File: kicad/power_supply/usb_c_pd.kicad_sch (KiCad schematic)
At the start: 39 parts, among them J201 Conn_01x04_Socket, J202 12401826E412A, J203 Conn_01x03_Socket, SW201 SW_SPST, U201 USBLC6-2SC6, U202 STUSB4500QTR

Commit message: psu buck-boost schematic capture
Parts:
- removed J203: Conn_01x03_Socket, symbol Connector:Conn_01x03_Socket
- added J203: USB IDC, symbol Connector:Conn_01x05_Pin
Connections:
- net D_N: now also J203.2 (Pin_2)
- net D_P: now also J203.3 (Pin_3)
- net GND: now also J203.4 (Pin_4), J203.5 (Pin_5)
- no-connect marks 12 -> 13
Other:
- note added: "Black"
- note added: "Green"
- note added: "Red"
- note added: "White"
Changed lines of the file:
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@@
 	)
 	(junction
+		(at 140.97 184.15)
+		(diameter 0)
+		(color 0 0 0 0)
+	)
+	(junction
 		(at 227.33 43.18)
 		(diameter 0)
@@
 	)
 	(no_connect
+		(at 139.7 173.99)
+	)
+	(no_connect
 		(at 137.16 130.81)
 	)
@@
 	(wire
 		(pts
-			(xy 142.24 179.07) (xy 135.89 179.07)
+			(xy 146.05 179.07) (xy 139.7 179.07)
 		)
 		(stroke
@@
 	(wire
 		(pts
+			(xy 140.97 181.61) (xy 140.97 184.15)
+		)
+		(stroke
+			(width 0)
+			(type default)
+		)
+	)
+	(wire
+		(pts
 			(xy 90.17 35.56) (xy 85.09 35.56)
 		)
@@
 	(wire
 		(pts
-			(xy 142.24 176.53) (xy 135.89 176.53)
+			(xy 146.05 176.53) (xy 139.7 176.53)
 		)
 		(stroke
@@
 	(wire
 		(pts
+			(xy 139.7 181.61) (xy 140.97 181.61)
+		)
+		(stroke
+			(width 0)
+			(type default)
+		)
+	)
+	(wire
+		(pts
 			(xy 22.86 39.37) (xy 22.86 40.64)
 		)
@@
 	(wire
 		(pts
-			(xy 135.89 181.61) (xy 137.16 181.61)
+			(xy 139.7 184.15) (xy 140.97 184.15)
 		)
 		(stroke
@@
 	(wire
 		(pts
-			(xy 137.16 181.61) (xy 137.16 182.88)
+			(xy 140.97 184.15) (xy 140.97 185.42)
 		)
 		(stroke
@@
 		)
 	)
+	(text "Black"
+		(exclude_from_sim no)
+		(at 131.318 184.404 0)
+		(effects
+			(font
+				(size 1.27 1.27)
+			)
+		)
+	)
+	(text "Green"
+		(exclude_from_sim no)
+		(at 131.318 179.324 0)
+		(effects
+			(font
+				(size 1.27 1.27)
+			)
+		)
+	)
 	(text "Reset Switch"
 		(exclude_from_sim no)
@@
 		)
 	)
+	(text "Red"
+		(exclude_from_sim no)
+		(at 130.556 174.244 0)
+		(effects
+			(font
+				(size 1.27 1.27)
+			)
+		)
+	)
 	(text "USB Header"
 		(exclude_from_sim no)
@@
 		)
 	)
+	(text "Black"
+		(exclude_from_sim no)
+		(at 131.318 181.864 0)
+		(effects
+			(font
+				(size 1.27 1.27)
+			)
+		)
+	)
+	(text "White"
+		(exclude_from_sim no)
+		(at 131.318 176.784 0)
+		(effects
+			(font
+				(size 1.27 1.27)
+			)
+		)
+	)
 	(text "ADDR0 | ADDR1 | Address\n  0    |   0    | 0x28*\n  0    |   1    | 0x29\n  1    |   0    | 0x2A\n  1    |   1    | 0x2B\n\n*: Default\n0: Jumper closed\n1: Jumper open"
 		(exclude_from_sim no)
@@
 	)
 	(label "D_P"
-		(at 142.24 179.07 180)
+		(at 146.05 179.07 180)
 		(fields_autoplaced yes)
 		(effects
@@
 	)
 	(label "D_N"
-		(at 142.24 176.53 180)
+		(at 146.05 176.53 180)
 		(fields_autoplaced yes)
 		(effects
@@
 	)
 	(symbol
+		(lib_id "Connector:Conn_01x05_Pin")
+		(at 134.62 179.07 0)
+		(unit 1)
+		(exclude_from_sim no)
+		(in_bom yes)
+		(on_board yes)
+		(dnp no)
+		(property "Reference" "J203"
+			(at 135.382 168.148 0)
+			(effects
+				(font
+					(size 1.27 1.27)
+				)
+			)
+		)
+		(property "Value" "USB IDC"
+			(at 135.382 170.688 0)
+			(effects
+				(font
+					(size 1.27 1.27)
+				)
+			)
+		)
+		(property "Footprint" ""
+			(at 134.62 179.07 0)
+			(effects
+				(font
+					(size 1.27 1.27)
+				)
+				(hide yes)
+			)
+		)
+		(property "Datasheet" "~"
+			(at 134.62 179.07 0)
+			(effects
+				(font
+					(size 1.27 1.27)
+				)
+				(hide yes)
+			)
+		)
+		(property "Description" "Generic connector, single row, 01x05, script generated"
+			(at 134.62 179.07 0)
+			(effects
+				(font
+					(size 1.27 1.27)
+				)
+				(hide yes)
+			)
+		)
+		(pin "3"
+		)
+		(pin "1"
+		)
+		(pin "4"
+		)
+		(pin "2"
+		)
+		(pin "5"
+		)
+		(instances
+			(project ""
+				(path "/6a7d9dc9-f78f-470f-911b-b95256023173/4a384965-6a35-4bf6-849e-cb865e62d5b4"
+					(reference "J203")
+					(unit 1)
+				)
+			)
+		)
+	)
+	(symbol
 		(lib_id "Device:R_Small_US")
 		(at 260.35 57.15 0)
@@
 	(symbol
 		(lib_id "power:GND")
-		(at 137.16 182.88 0)
+		(at 140.97 185.42 0)
 		(unit 1)
 		(exclude_from_sim no)
@@
 		(fields_autoplaced yes)
 		(property "Reference" "#PWR0206"
-			(at 137.16 189.23 0)
+			(at 140.97 191.77 0)
 			(effects
 				(font
@@
 		)
 		(property "Value" "GND"
-			(at 137.16 187.96 0)
+			(at 140.97 190.5 0)
 			(effects
 				(font
@@
 		)
 		(property "Footprint" ""
-			(at 137.16 182.88 0)
+			(at 140.97 185.42 0)
 			(effects
 				(font
@@
 		)
 		(property "Datasheet" ""
-			(at 137.16 182.88 0)
+			(at 140.97 185.42 0)
 			(effects
 				(font
@@
 		)
 		(property "Description" "Power symbol creates a global label with name \"GND\" , ground"
-			(at 137.16 182.88 0)
+			(at 140.97 185.42 0)
 			(effects
 				(font
@@
 					(unit 1)
 				)
-			)
-		)
-	)
-	(symbol
-		(lib_id "Connector:Conn_01x03_Socket")
-		(at 130.81 179.07 180)
-		(unit 1)
-		(exclude_from_sim no)
-		(in_bom yes)
-		(on_board yes)
-		(dnp no)
-		(property "Reference" "J203"
-			(at 133.35 172.466 0)
-			(effects
-				(font
-					(size 1.27 1.27)
-				)
-			)
-		)
-		(property "Value" "Conn_01x03_Socket"
-			(at 131.445 173.99 0)
-			(effects
-				(font
-					(size 1.27 1.27)
-				)
-				(hide yes)
-			)
-		)
-		(property "Footprint" ""
-			(at 130.81 179.07 0)
-			(effects
-				(font
-					(size 1.27 1.27)
-				)
-				(hide yes)
-			)
-		)
-		(property "Datasheet" "~"
-			(at 130.81 179.07 0)
-			(effects
-				(font
-					(size 1.27 1.27)
-				)
-				(hide yes)
-			)
-		)
-		(property "Description" "Generic connector, single row, 01x03, script generated"
-			(at 130.81 179.07 0)
-			(effects
-				(font
-					(size 1.27 1.27)
-				)
-				(hide yes)
-			)
-		)
-		(pin "3"
-		)
-		(pin "1"
-		)
-		(pin "2"
-		)
-		(instances
-			(project ""
-				(path "/6a7d9dc9-f78f-470f-911b-b95256023173/4a384965-6a35-4bf6-849e-cb865e62d5b4"
-					(reference "J203")
-					(unit 1)
-				)

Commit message: schematic capture
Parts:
- J202: MPN (none) -> 12401826E412A
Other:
- moved on the sheet: TP201
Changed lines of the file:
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@@
 	(wire
 		(pts
-			(xy 161.29 101.6) (xy 171.45 101.6)
+			(xy 163.83 101.6) (xy 171.45 101.6)
 		)
 		(stroke
@@
 	)
 	(symbol
-		(lib_name "SISA35DN-T1-GE3_1")
 		(lib_id "SISA35DN-T1-GE3:SISA35DN-T1-GE3")
 		(at 220.98 45.72 270)
@@
 		(on_board yes)
 		(dnp no)
-		(fields_autoplaced yes)
 		(property "Reference" "J202"
 			(at 121.92 67.31 0)
@@
 					(size 1.27 1.27)
 				)
+				(hide yes)
 			)
 		)
@@
 			)
 		)
-		(property "Datasheet" "https://www.usb.org/sites/default/files/documents/usb_type-c.zip"
+		(property "Datasheet" "https://cdn.amphenol-cs.com/media/wysiwyg/files/documentation/datasheet/inputoutput/io_usb_type_c.pdf"
 			(at 125.73 100.33 0)
 			(effects
@@
 			)
 		)
-		(property "Description" "USB Full-Featured Type-C Receptacle connector"
+		(property "Description" "CONN RCP USB3.1 TYPEC 24P SMD RA"
 			(at 121.92 100.33 0)
 			(effects
@@
 			)
 		)
+		(property "MPN" "12401826E412A"
+			(at 121.92 70.358 0)
+			(effects
+				(font
+					(size 1.27 1.27)
+				)
+			)
+		)
 		(pin "A2"
 		)
@@
 	(symbol
 		(lib_id "Connector:TestPoint")
-		(at 161.29 101.6 90)
+		(at 163.83 101.6 90)
 		(unit 1)
 		(exclude_from_sim no)
@@
 		(dnp no)
 		(property "Reference" "TP201"
-			(at 156.464 101.6 90)
+			(at 159.004 101.6 90)
 			(effects
 				(font
@@
 		)
 		(property "Value" "TestPoint"
-			(at 156.21 100.3301 90)
+			(at 158.75 100.3301 90)
 			(effects
 				(font
@@
 		)
 		(property "Footprint" ""
-			(at 161.29 96.52 0)
+			(at 163.83 96.52 0)
 			(effects
 				(font
@@
 		)
 		(property "Datasheet" "~"
-			(at 161.29 96.52 0)
+			(at 163.83 96.52 0)
 			(effects
 				(font
@@
 		)
 		(property "Description" "test point"
-			(at 161.29 101.6 0)
+			(at 163.83 101.6 0)
 			(effects
 				(font

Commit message: schematic capture
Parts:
- removed TP202, TP203: TestPoint, symbol Connector:TestPoint
- renumbered TP204 to TP202, TP205 to TP203, TP206 to TP204
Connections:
- net POWER_OK3_OD: now reaches U202.14 (POWER_OK3)
- net POWER_OK2_OD: now reaches U202.20 (POWER_OK2)
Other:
- note added: "Required PDO configuration: PDO1 = Doesn't matter, the minimum VIN for the MP2759 is 6.6V to charge a 1-cell battery PDO2 = 9V, 2A (18W, 1-cell max.) PDO3 = 15V, 2A (30W, 3-cell max.) **Make sure to set the charger ILIM to the lowest current of PDO2 and PDO3**"
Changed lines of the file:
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@@
 		)
 	)
+	(text "Required PDO configuration:\n\nPDO1 = Doesn't matter, the minimum \n		VIN for the MP2759 is 6.6V \n		to charge a 1-cell battery\nPDO2 = 9V, 2A (18W, 1-cell max.)\nPDO3 = 15V, 2A (30W, 3-cell max.)\n\n\n**Make sure to set the charger ILIM\nto the lowest current of PDO2 and PDO3**"
+		(exclude_from_sim no)
+		(at 214.63 125.73 0)
+		(effects
+			(font
+				(size 1.905 1.905)
+			)
+			(justify left top)
+		)
+	)
 	(text "White"
 		(exclude_from_sim no)
@@
 		)
 	)
-	(hierarchical_label "VSNK"
+	(hierarchical_label "POWER_OK3_OD"
 		(shape input)
+		(at 204.47 88.9 0)
+		(fields_autoplaced yes)
+		(effects
+			(font
+				(size 1.27 1.27)
+			)
+			(justify left)
+		)
+	)
+	(hierarchical_label "POWER_OK2_OD"
+		(shape input)
+		(at 204.47 86.36 0)
+		(fields_autoplaced yes)
+		(effects
+			(font
+				(size 1.27 1.27)
+			)
+			(justify left)
+		)
+	)
+	(hierarchical_label "VSNK"
+		(shape output)
 		(at 267.97 43.18 0)
 		(fields_autoplaced yes)
@@
 		(on_board yes)
 		(dnp no)
-		(property "Reference" "TP206"
+		(property "Reference" "TP204"
 			(at 209.296 104.14 90)
 			(effects
@@
 			(project "power_supply"
 				(path "/6a7d9dc9-f78f-470f-911b-b95256023173/4a384965-6a35-4bf6-849e-cb865e62d5b4"
-					(reference "TP206")
+					(reference "TP204")
 					(unit 1)
 				)
@@
 		(on_board yes)
 		(dnp no)
-		(property "Reference" "TP205"
+		(property "Reference" "TP203"
 			(at 209.296 101.6 90)
 			(effects
@@
 			(project "power_supply"
 				(path "/6a7d9dc9-f78f-470f-911b-b95256023173/4a384965-6a35-4bf6-849e-cb865e62d5b4"
-					(reference "TP205")
+					(reference "TP203")
 					(unit 1)
 				)
@@
 	)
 	(symbol
-		(lib_id "Connector:TestPoint")
-		(at 204.47 88.9 270)
-		(unit 1)
-		(exclude_from_sim no)
-		(in_bom yes)
-		(on_board yes)
-		(dnp no)
-		(property "Reference" "TP203"
-			(at 209.296 88.9 90)
-			(effects
-				(font
-					(size 1.27 1.27)
-				)
-				(justify left)
-			)
-		)
-		(property "Value" "TestPoint"
-			(at 209.55 90.1699 90)
-			(effects
-				(font
-					(size 1.27 1.27)
-				)
-				(justify left)
-				(hide yes)
-			)
-		)
-		(property "Footprint" ""
-			(at 204.47 93.98 0)
-			(effects
-				(font
-					(size 1.27 1.27)
-				)
-				(hide yes)
-			)
-		)
-		(property "Datasheet" "~"
-			(at 204.47 93.98 0)
-			(effects
-				(font
-					(size 1.27 1.27)
-				)
-				(hide yes)
-			)
-		)
-		(property "Description" "test point"
-			(at 204.47 88.9 0)
-			(effects
-				(font
-					(size 1.27 1.27)
-				)
-				(hide yes)
-			)
-		)
-		(pin "1"
-		)
-		(instances
-			(project "power_supply"
-				(path "/6a7d9dc9-f78f-470f-911b-b95256023173/4a384965-6a35-4bf6-849e-cb865e62d5b4"
-					(reference "TP203")
-					(unit 1)
-				)
-			)
-		)
-	)
-	(symbol
 		(lib_id "power:GND")
 		(at 209.55 66.04 0)
@@
 	)
 	(symbol
-		(lib_id "Connector:TestPoint")
-		(at 204.47 86.36 270)
-		(unit 1)
-		(exclude_from_sim no)
-		(in_bom yes)
-		(on_board yes)
-		(dnp no)
-		(property "Reference" "TP202"
-			(at 209.296 86.36 90)
-			(effects
-				(font
-					(size 1.27 1.27)
-				)
-				(justify left)
-			)
-		)
-		(property "Value" "TestPoint"
-			(at 209.55 87.6299 90)
-			(effects
-				(font
-					(size 1.27 1.27)
-				)
-				(justify left)
-				(hide yes)
-			)
-		)
-		(property "Footprint" ""
-			(at 204.47 91.44 0)
-			(effects
-				(font
-					(size 1.27 1.27)
-				)
-				(hide yes)
-			)
-		)
-		(property "Datasheet" "~"
-			(at 204.47 91.44 0)
-			(effects
-				(font
-					(size 1.27 1.27)
-				)
-				(hide yes)
-			)
-		)
-		(property "Description" "test point"
-			(at 204.47 86.36 0)
-			(effects
-				(font
-					(size 1.27 1.27)
-				)
-				(hide yes)
-			)
-		)
-		(pin "1"
-		)
-		(instances
-			(project "power_supply"
-				(path "/6a7d9dc9-f78f-470f-911b-b95256023173/4a384965-6a35-4bf6-849e-cb865e62d5b4"
-					(reference "TP202")
-					(unit 1)
-				)
-			)
-		)
-	)
-	(symbol
 		(lib_id "power:GND")
 		(at 186.69 113.03 0)
@@
 		(on_board yes)
 		(dnp no)
-		(property "Reference" "TP204"
+		(property "Reference" "TP202"
 			(at 209.296 99.06 90)
 			(effects
@@
 			(project "power_supply"
 				(path "/6a7d9dc9-f78f-470f-911b-b95256023173/4a384965-6a35-4bf6-849e-cb865e62d5b4"
-					(reference "TP204")
+					(reference "TP202")
 					(unit 1)
 				)

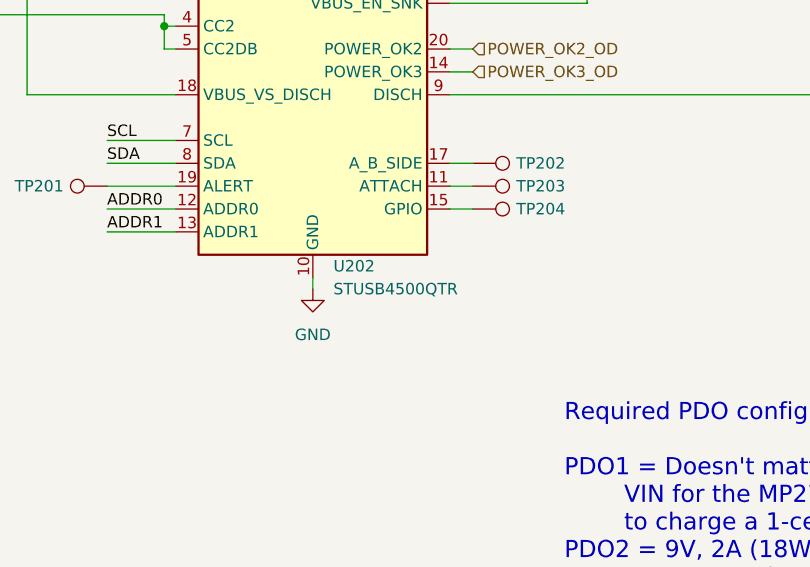
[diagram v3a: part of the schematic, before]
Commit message: improved load switch mosfet paste aperture
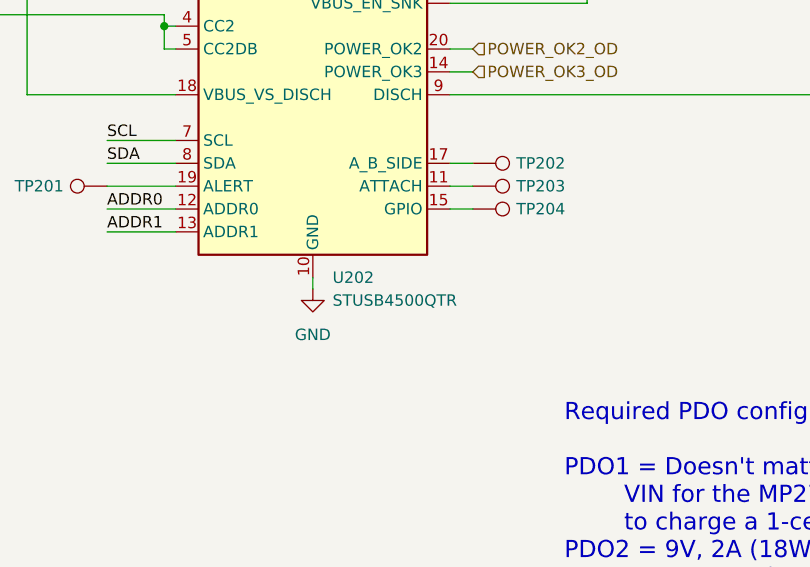
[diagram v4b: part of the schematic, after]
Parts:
- U202: value STUSB4500QTR -> ~; MPN (none) -> STUSB4500QTR
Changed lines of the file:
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@@
-	)
-	(symbol
-		(lib_id "STUSB4500QTR:STUSB4500QTR")
-		(at 186.69 88.9 0)
-		(unit 1)
-		(exclude_from_sim no)
-		(in_bom yes)
-		(on_board yes)
-		(dnp no)
-		(property "Reference" "U202"
-			(at 188.976 110.49 0)
-			(effects
-				(font
-					(size 1.27 1.27)
-				)
-				(justify left)
-			)
-		)
-		(property "Value" "STUSB4500QTR"
-			(at 188.976 113.03 0)
-			(effects
-				(font
-					(size 1.27 1.27)
-				)
-				(justify left)
-			)
-		)
-		(property "Footprint" "Package_DFN_QFN:QFN-24-1EP_4x4mm_P0.5mm_EP2.7x2.7mm"
-			(at 186.69 50.546 0)
-			(effects
-				(font
-					(size 1.27 1.27)
-				)
-				(hide yes)
-			)
-		)
-		(property "Datasheet" "https://www.st.com/resource/en/datasheet/stusb4500.pdf"
-			(at 187.198 52.832 0)
-			(effects
-				(font
-					(size 1.27 1.27)
-				)
-				(hide yes)
-			)
-		)
-		(property "Description" "Stand-alone USB PD controller (with sink Auto-run mode), QFN-24"
-			(at 186.69 48.26 0)
-			(effects
-				(font
-					(size 1.27 1.27)
-				)
-				(hide yes)
-			)
-		)
-		(pin "15"
-		)
-		(pin "1"
-		)
-		(pin "20"
-		)
-		(pin "8"
-		)
-		(pin "22"
-		)
-		(pin "2"
-		)
-		(pin "10"
-		)
-		(pin "5"
-		)
-		(pin "24"
-		)
-		(pin "4"
-		)
-		(pin "7"
-		)
-		(pin "14"
-		)
-		(pin "19"
-		)
-		(pin "21"
-		)
-		(pin "17"
-		)
-		(pin "9"
-		)
-		(pin "18"
-		)
-		(pin "16"
-		)
-		(pin "25"
-		)
-		(pin "13"
-		)
-		(pin "12"
-		)
-		(pin "3"
-		)
-		(pin "23"
-		)
-		(pin "6"
-		)
-		(pin "11"
-		)
-		(instances
-			(project "power_supply"
-				(path "/6a7d9dc9-f78f-470f-911b-b95256023173/4a384965-6a35-4bf6-849e-cb865e62d5b4"
-					(reference "U202")
-					(unit 1)
-				)
-			)
-		)
 	)
 	(symbol
@@
 					(unit 1)
 				)
+			)
+		)
+	)
+	(symbol
+		(lib_id "STUSB4500QTR:STUSB4500QTR")
+		(at 186.69 88.9 0)
+		(unit 1)
+		(exclude_from_sim no)
+		(in_bom yes)
+		(on_board yes)
+		(dnp no)
+		(fields_autoplaced yes)
+		(property "Reference" "U202"
+			(at 188.8841 111.76 0)
+			(effects
+				(font
+					(size 1.27 1.27)
+				)
+				(justify left)
+			)
+		)
+		(property "Value" "~"
+			(at 195.58 110.49 0)
+			(effects
+				(font
+					(size 1.27 1.27)
+				)
+				(hide yes)
+			)
+		)
+		(property "Footprint" "Package_DFN_QFN:QFN-24-1EP_4x4mm_P0.5mm_EP2.7x2.7mm"
+			(at 186.944 52.578 0)
+			(effects
+				(font
+					(size 1.27 1.27)
+				)
+				(hide yes)
+			)
+		)
+		(property "Datasheet" "https://www.st.com/resource/en/datasheet/stusb4500.pdf"
+			(at 186.436 49.276 0)
+			(effects
+				(font
+					(size 1.27 1.27)
+				)
+				(hide yes)
+			)
+		)
+		(property "Description" "Stand-alone USB PD controller (with sink Auto-run mode), QFN-24"
+			(at 186.436 46.228 0)
+			(effects
+				(font
+					(size 1.27 1.27)
+				)
+				(hide yes)
+			)
+		)
+		(property "MPN" "STUSB4500QTR"
+			(at 188.8841 114.3 0)
+			(effects
+				(font
+					(size 1.27 1.27)
+				)
+				(justify left)
+			)
+		)
+		(pin "7"
+		)
+		(pin "9"
+		)
+		(pin "12"
+		)
+		(pin "15"
+		)
+		(pin "23"
+		)
+		(pin "10"
+		)
+		(pin "16"
+		)
+		(pin "17"
+		)
+		(pin "18"
+		)
+		(pin "25"
+		)
+		(pin "24"
+		)
+		(pin "8"
+		)
+		(pin "2"
+		)
+		(pin "14"
+		)
+		(pin "21"
+		)
+		(pin "22"
+		)
+		(pin "1"
+		)
+		(pin "20"
+		)
+		(pin "3"
+		)
+		(pin "4"
+		)
+		(pin "13"
+		)
+		(pin "19"
+		)
+		(pin "6"
+		)
+		(pin "11"
+		)
+		(pin "5"
+		)
+		(instances
+			(project ""
+				(path "/6a7d9dc9-f78f-470f-911b-b95256023173/4a384965-6a35-4bf6-849e-cb865e62d5b4"
+					(reference "U202")
+					(unit 1)
+				)
